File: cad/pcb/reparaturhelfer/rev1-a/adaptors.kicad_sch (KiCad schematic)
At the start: 64 parts, among them J401 Conn_01x01, J402 Conn_01x01, J403 Conn_01x01, J404 Conn_01x01, J405 Conn_01x01, J406 Conn_01x01, J407 Conn_01x01, J408 Conn_01x01, J409 Conn_01x01, J410 Conn_01x01, J411 Conn_01x01, J412 Conn_01x01, J413 Conn_01x01, J414 Conn_01x01, J415 Conn_01x01, J416 Conn_01x01, J417 Conn_01x01, J418 Conn_01x01, J419 Conn_01x01, J420 Conn_01x01, J421 Conn_01x01, J422 Conn_01x01, J423 Conn_01x01, J424 Conn_01x01, J425 Conn_01x01, J426 Conn_01x01, J427 Conn_01x01, J428 Conn_01x01, J429 Conn_01x01, J430 Conn_01x01, J431 Conn_01x01, J432 Conn_01x01, J433 Conn_01x01, J434 Conn_01x01, J435 Conn_01x01, J436 Conn_01x01, J437 Conn_01x01, J438 Conn_01x01, J439 Conn_01x01, J440 Conn_01x01, J441 Conn_01x01, J442 Conn_01x01

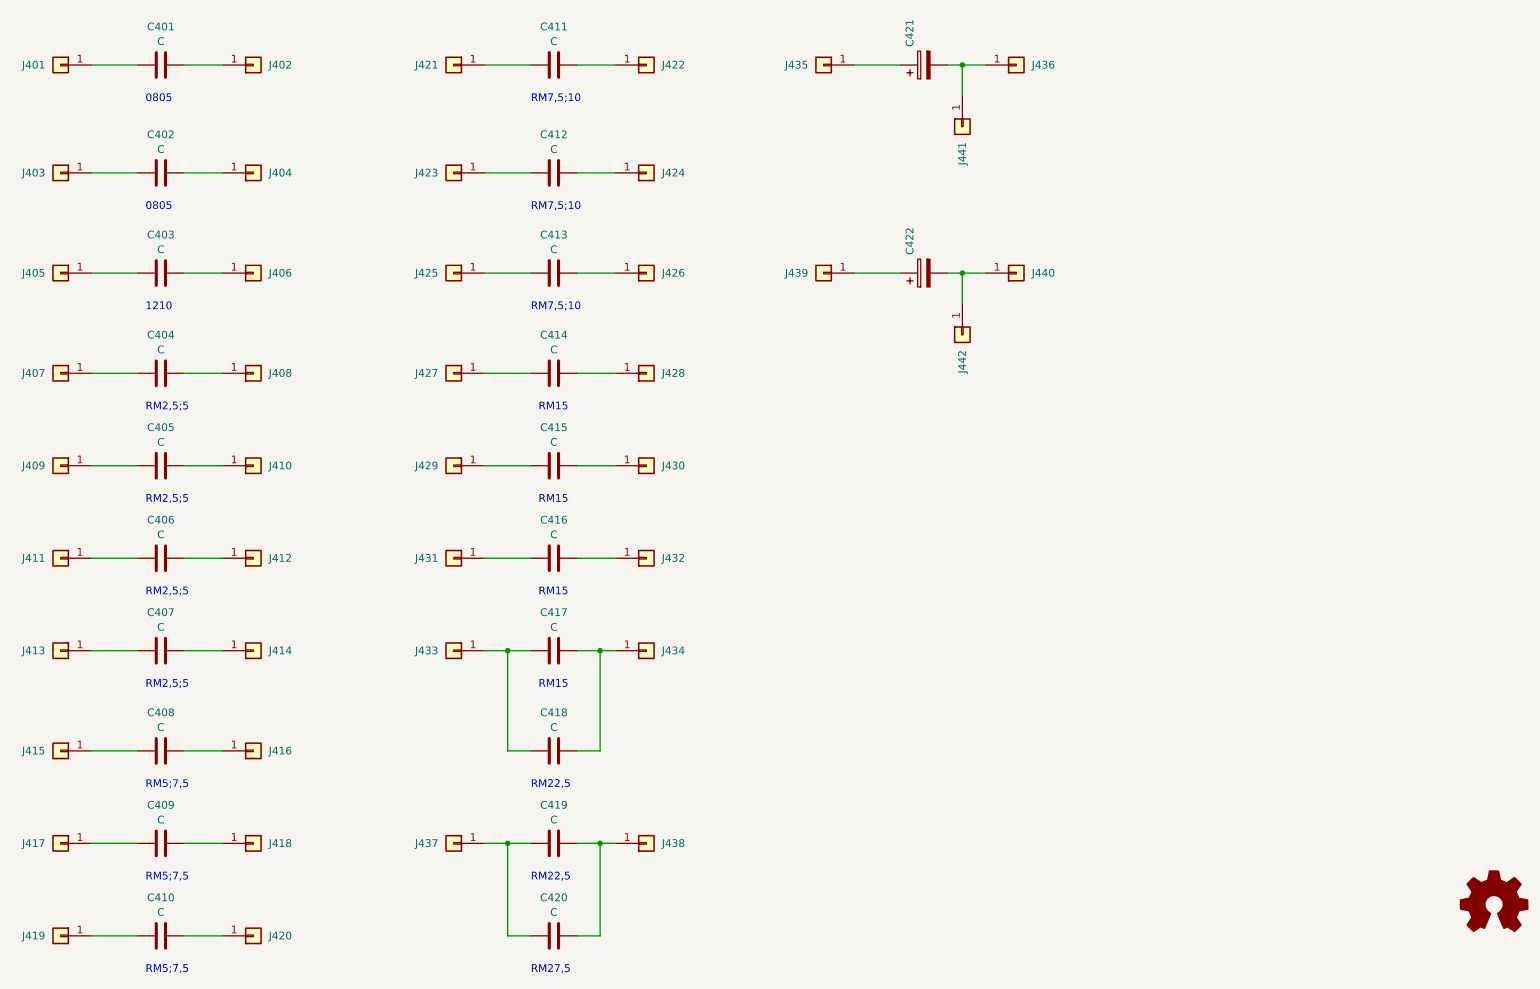
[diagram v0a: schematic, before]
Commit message: Add: Routing Bluetooth
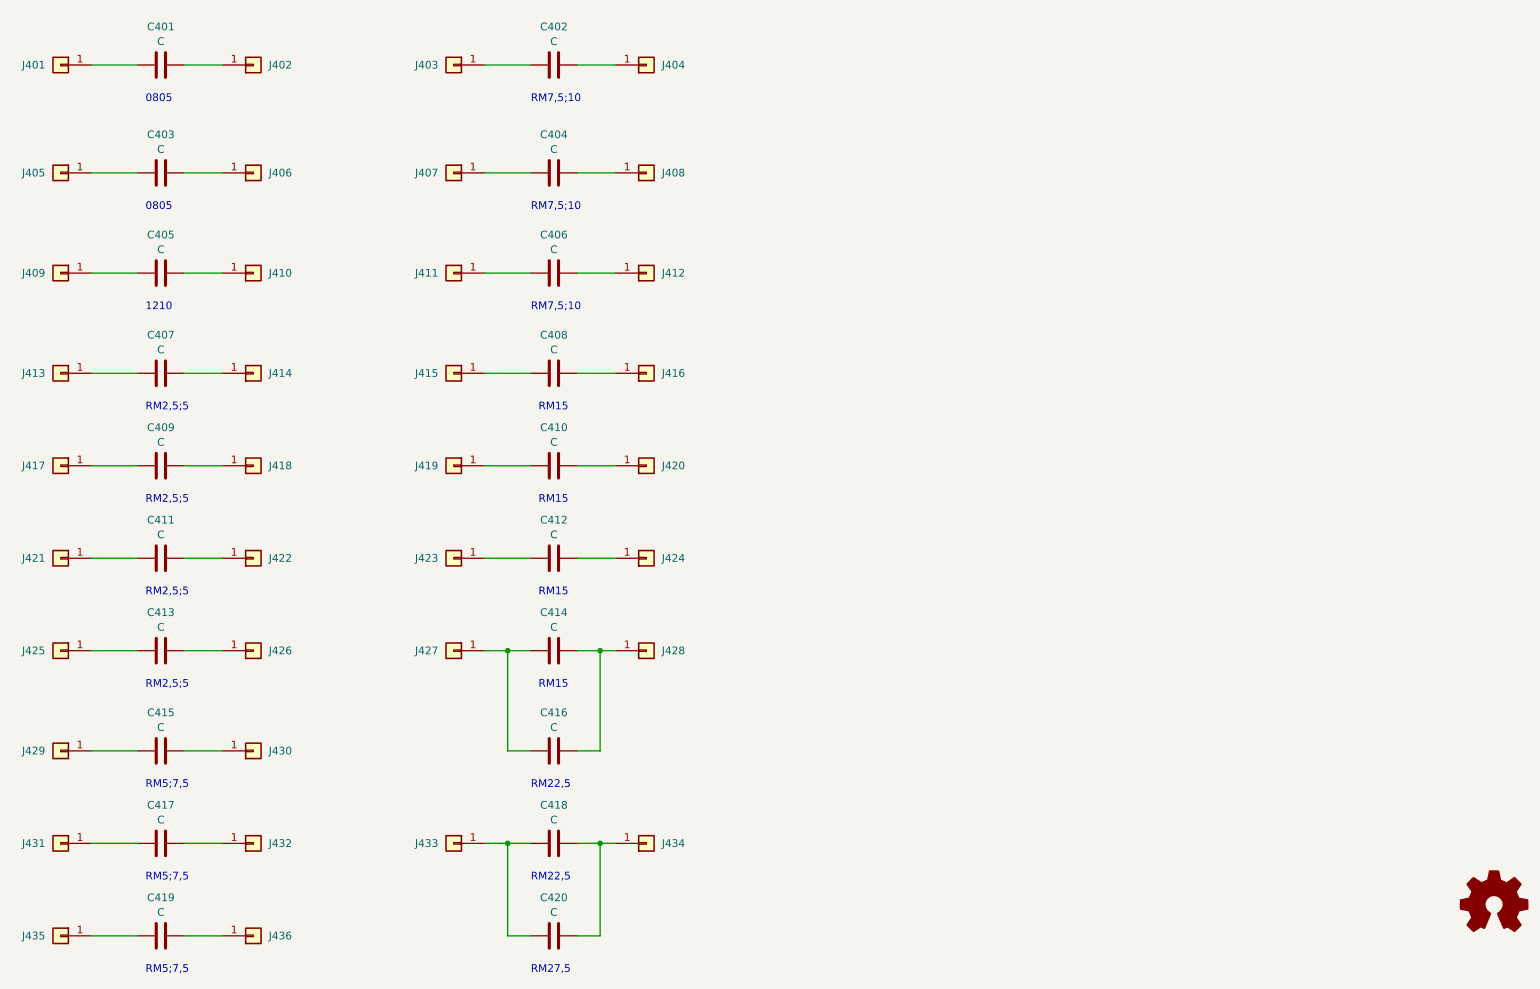
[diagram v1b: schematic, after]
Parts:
- removed C421: ~, Capacitor_THT:CP_Radial_D8.0mm_P5.00mm, symbol saba-fernbedienung-rescue:CP-Device
- removed C422: ~, Capacitor_THT:CP_Radial_D10.0mm_P7.50mm, symbol saba-fernbedienung-rescue:CP-Device
- removed J435, J436, J439, J440, J441, J442: Conn_01x01, Connector_PinHeader_2.54mm:PinHeader_1x01_P2.54mm_Vertical, symbol Connector_Generic:Conn_01x01
- renumbered C411 to C402, C402 to C403, C412 to C404, C403 to C405, C413 to C406, C404 to C407, C414 to C408, C405 to C409, C415 to C410, C406 to C411, C416 to C412, C407 to C413, C417 to C414, C408 to C415, C418 to C416, C409 to C417, C419 to C418, C410 to C419, J421 to J403, J422 to J404, J403 to J405, J404 to J406, J423 to J407, J424 to J408, J405 to J409, J406 to J410, J425 to J411, J426 to J412, J407 to J413, J408 to J414, J427 to J415, J428 to J416, J409 to J417, J410 to J418, J429 to J419, J430 to J420, J411 to J421, J412 to J422, J431 to J423, J432 to J424, J413 to J425, J414 to J426, J433 to J427, J434 to J428, J415 to J429, J416 to J430, J417 to J431, J418 to J432, J437 to J433, J438 to J434, J419 to J435, J420 to J436

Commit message: Add: PCB fertig
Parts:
- C412: footprint Capacitor_THT:C_Rect_L16.5mm_W7.0mm_P15.00mm_MKT -> Capacitor_THT:C_Rect_L7.0mm_W3.5mm_P2.50mm_P5.00mm
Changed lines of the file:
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@@
       (effects (font (size 1.27 1.27)))
     )
-    (property "Footprint" "Capacitor_THT:C_Rect_L16.5mm_W7.0mm_P15.00mm_MKT" (at 125.73 115.8748 0)
+    (property "Footprint" "Capacitor_THT:C_Rect_L7.0mm_W3.5mm_P2.50mm_P5.00mm" (at 125.73 115.8748 0)
       (effects (font (size 1.27 1.27)) hide)
     )
